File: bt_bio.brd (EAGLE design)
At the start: 57.8 x 57.9 mm, 75 parts, among them U1 ADP121-AUJZ33R7, U2 MCP73837-FCI/UN, U4 ADP121-AUJZ18R7, U5 LSM9DS1, X1 53047-03, X2 MINI-USB-SHIELD-UX60-MB-5ST, X3 53047-03

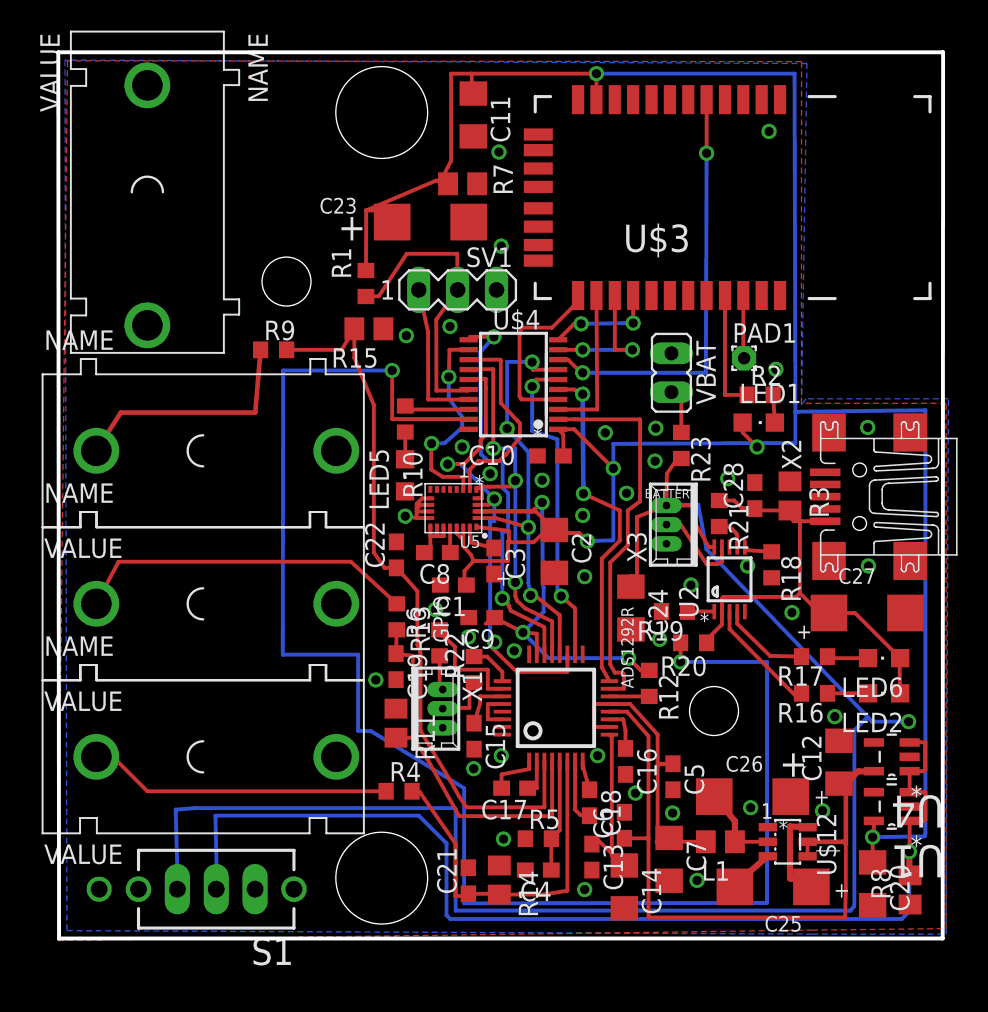
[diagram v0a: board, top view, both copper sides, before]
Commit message: switched to RN4678
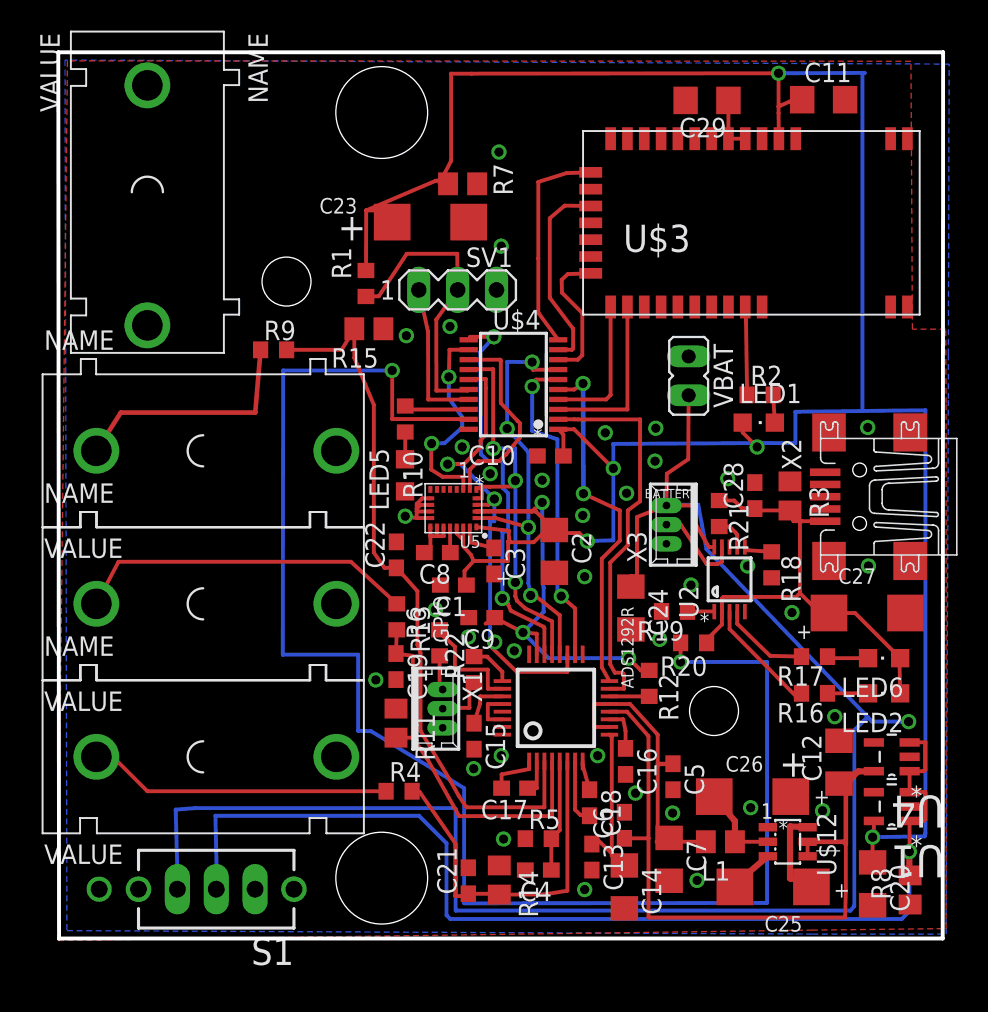
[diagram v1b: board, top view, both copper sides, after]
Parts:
- removed PAD1: WIREPAD1,6/0,8, wirepad:1,6/0,8
- removed R23: 51K, rcl:R0603
- removed U$3: RN42, RN42__BoB:SPARKFUN_RN41
- added C29: 1uF, rcl:C1206
- added U$1: RN4678, rn4678:RN4678
- R2: value 2.2K -> 2K2
- moved C11 22.9 mm to (50.6, 55.5), turned to 0 degrees
- moved VBAT 1.14 mm to (41.8, 37.4)
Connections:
- removed net N$10: R2.1, U$3.21
- removed net N$14: PAD1.1, U$3.22
- removed net N$46: C24.1, R23.2, S1.3, U2.10, X3.1
- removed net N$7: U$3.15, U$4.9
- removed net N$8: U$3.16, U$4.10
- removed net N$9: U$3.5, U$4.8
- new net CTS: U$1.15, U$4.10
- new net RESET: U$1.21, U$4.8
- new net RTS: U$1.17, U$4.9
- new net RX: U$1.22, U$4.4
- new net TX: U$1.23, U$4.3
- net GND: now also C29.2, U$1.1, U$1.2, U$1.20, U$1.3, U$1.31, U$1.32, U$1.33; no longer U$3.1, U$3.12, U$3.28, U$3.29
- net N$2: now also C29.1, U$1.6, U$1.7; no longer U$3.13, U$4.4
- net N$31: now also C24.1, S1.3, U2.10, X3.1; no longer R23.1
- net N$6: now also R2.1, U$1.30; no longer U$3.14, U$4.3
- net V+: now also U$1.4; no longer U$3.11
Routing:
- net N$31: track 3.28 -> 112.4 mm, vias 0 -> 1
- net N$46: track 108.0 -> 0.00 mm, vias 1 -> 0
- net N$9: track 28.0 -> 0.00 mm, vias 2 -> 0
- net CTS: track 0.00 -> 14.3 mm
- net RTS: track 0.00 -> 13.0 mm
- net TX: track 0.00 -> 11.2 mm
- net N$7: track 9.55 -> 0.00 mm, vias 2 -> 0
- net RX: track 0.00 -> 9.30 mm
- net RESET: track 0.00 -> 9.22 mm
- net N$2: track 11.9 -> 3.60 mm
- net N$10: track 7.95 -> 0.00 mm
- net V+: track 192.3 -> 199.8 mm
- net N$8: track 7.13 -> 0.00 mm, vias 2 -> 0
- net N$14: track 4.15 -> 0.00 mm
- net N$6: track 10.0 -> 5.95 mm
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
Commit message: Small fixes in the layout
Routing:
- net GND: vias 36 -> 37
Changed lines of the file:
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@@
 <contactref element="U$1" pad="20"/>
 <contactref element="C29" pad="2"/>
+<via x="33.678" y="45.201" extent="1-16" drill="0.6" shape="octagon"/>
 </signal>
 <signal name="+5V">
@@
 <via x="36.85" y="31.35" extent="1-16" drill="0.6" shape="octagon"/>
 <via x="47.65" y="57.175" extent="1-16" drill="0.6" shape="octagon"/>
-<wire x1="47.65" y1="57.175" x2="53.275" y2="57.2" width="0.254" layer="16"/>
+<wire x1="47.65" y1="57.175" x2="48.2" y2="57.175" width="0.254" layer="16"/>
 <wire x1="48.75" y1="33" x2="46.5000375" y2="33.009621875" width="0.254" layer="16"/>
 <wire x1="46.5000375" y1="33.009621875" x2="36.85" y2="32.95" width="0.254" layer="16"/>
@@
 <wire x1="49.2" y1="55.45" x2="48.375" y2="55.325" width="0.254" layer="1"/>
 <wire x1="48.375" y1="55.325" x2="47.65" y2="55" width="0.254" layer="1"/>
-<wire x1="53.275" y1="57.2" x2="53.131453125" y2="57.2" width="0.254" layer="16"/>
+<wire x1="48.2" y1="57.175" x2="53.131453125" y2="57.2" width="0.254" layer="16"/>
 <wire x1="53.131453125" y1="57.2" x2="53.131453125" y2="35.101546875" width="0.254" layer="16"/>
 </signal>

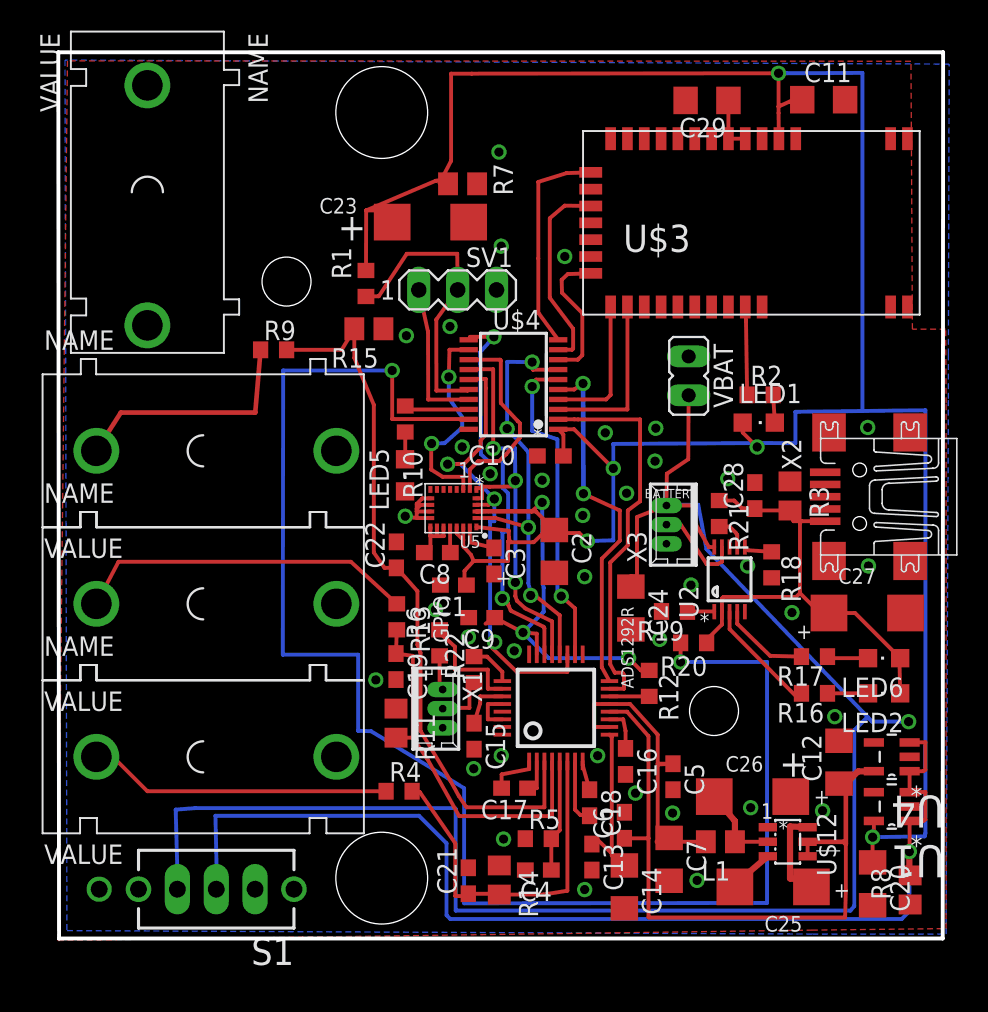
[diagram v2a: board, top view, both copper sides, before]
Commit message: Tested with actual bluetooth module and it seems to work.
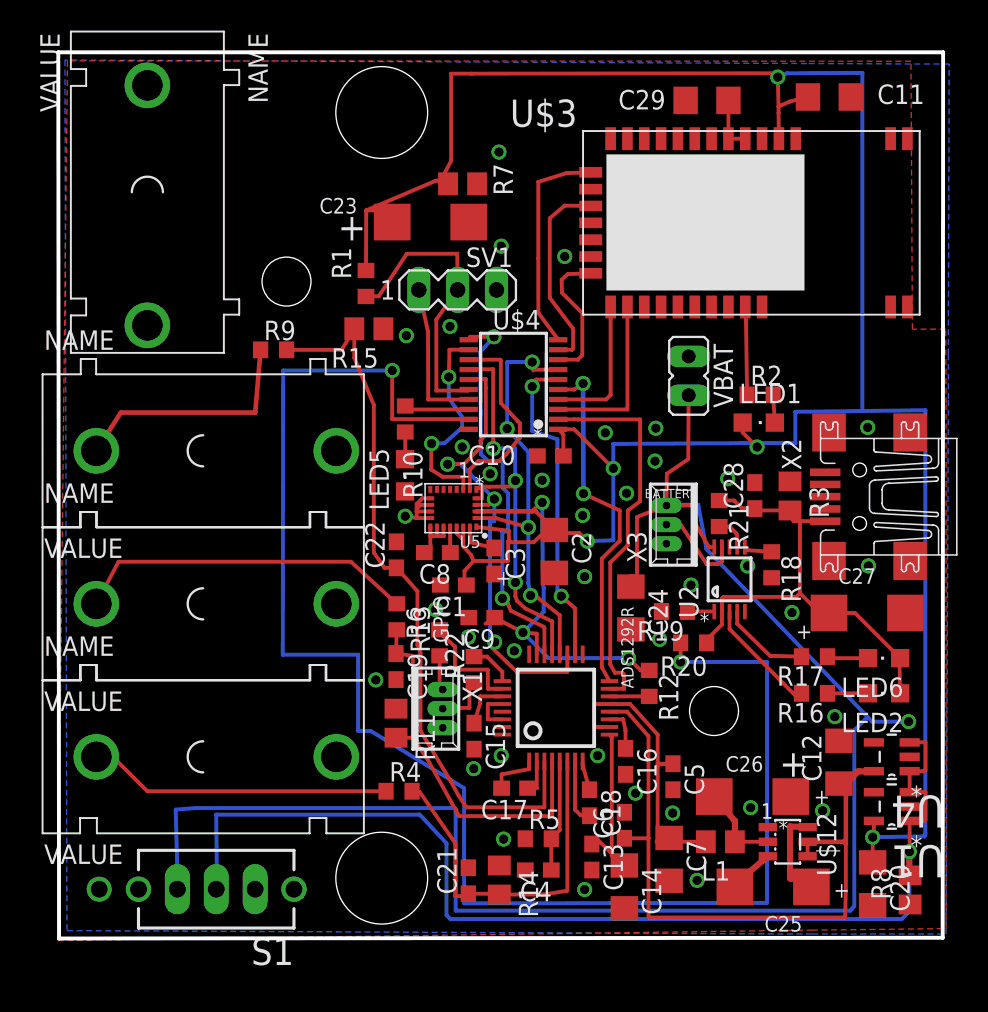
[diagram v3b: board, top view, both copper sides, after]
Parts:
- moved C11 0.41 mm to (51.0, 55.6)
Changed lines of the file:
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@@
 <board>
 <plain>
-<wire x1="0.627" y1="0.627" x2="58.379" y2="0.627" width="0.254" layer="20"/>
-<wire x1="58.379" y1="0.627" x2="58.406" y2="58.545" width="0.254" layer="20"/>
+<wire x1="0.627" y1="0.627" x2="58.379" y2="0.677" width="0.254" layer="20"/>
+<wire x1="58.379" y1="0.677" x2="58.406" y2="58.545" width="0.254" layer="20"/>
 <wire x1="58.406" y1="58.545" x2="0.577" y2="58.545" width="0.254" layer="20"/>
 <wire x1="0.577" y1="58.545" x2="0.627" y2="0.627" width="0.254" layer="20"/>
@@
 <hole x="21.717" y="54.61" drill="6"/>
 <text x="37.55" y="48.2" size="1.778" layer="27">RN42</text>
-<text x="37.5" y="45.5" size="1.778" layer="25">U$3</text>
+<text x="30.1" y="53.675" size="1.778" layer="25">U$3</text>
 <text x="26.7" y="30.75" size="1.016" layer="25">1</text>
 <text x="46.5" y="8.45" size="1.016" layer="25">1</text>
@@
 <text x="38.9" y="29.4" size="0.6096" layer="25">BATTERY</text>
 <text x="26.1" y="19.95" size="1.016" layer="25" rot="R90">GPIO</text>
+<rectangle x1="36.4" y1="42.975" x2="49.35" y2="51.875" layer="25"/>
 </plain>
 <attributes>
@@
 <element name="C12" library="rcl" package="C1206" value="10uF" x="51.6" y="12.15" rot="R90"/>
 <element name="C20" library="rcl" package="C1206" value="10uF" x="53.8" y="4.2" rot="R270"/>
-<element name="C11" library="rcl" package="C1206" value="10uF" x="50.6" y="55.45"/>
+<element name="C11" library="rcl" package="C1206" value="10uF" x="50.975" y="55.625" smashed="yes">
+<attribute name="NAME" x="54.105" y="55.168" size="1.27" layer="25"/>
+<attribute name="VALUE" x="49.705" y="53.212" size="1.27" layer="27"/>
+</element>
 <element name="C23" library="rcl" package="SMC_C" value="4.7uF" x="24.9" y="47.45" smashed="yes">
 <attribute name="NAME" x="17.645" y="48.005" size="1.016" layer="25"/>
@@
 <element name="C24" library="rcl" package="C1206" value="10uF" x="38" y="22.225" rot="R270"/>
 <element name="U$1" library="rn4678" package="RN4678" value="RN4678" x="34.875" y="53.4" rot="R270"/>
-<element name="C29" library="rcl" package="C1206" value="1uF" x="42.975" y="55.4" rot="R180"/>
+<element name="C29" library="rcl" package="C1206" value="1uF" x="42.975" y="55.4" smashed="yes" rot="R180">
+<attribute name="NAME" x="40.27" y="56.082" size="1.27" layer="25" rot="R180"/>
+<attribute name="VALUE" x="44.245" y="57.813" size="1.27" layer="27" rot="R180"/>
+</element>
 </elements>
 <signals>
@@
 <wire x1="33.201" y1="33.876" x2="33.251" y2="33.907" width="0.254" layer="1"/>
 <via x="36.85" y="31.35" extent="1-16" drill="0.6" shape="octagon"/>
-<via x="47.65" y="57.175" extent="1-16" drill="0.6" shape="octagon"/>
-<wire x1="47.65" y1="57.175" x2="48.2" y2="57.175" width="0.254" layer="16"/>
+<via x="47.6" y="56.925" extent="1-16" drill="0.6" shape="octagon"/>
+<wire x1="47.6" y1="56.925" x2="48.2" y2="57.175" width="0.254" layer="16"/>
 <wire x1="48.75" y1="33" x2="46.5000375" y2="33.009621875" width="0.254" layer="16"/>
 <wire x1="46.5000375" y1="33.009621875" x2="36.85" y2="32.95" width="0.254" layer="16"/>
@@
 <wire x1="26.25" y1="57.15" x2="27.6" y2="57.15" width="0.254" layer="1"/>
 <contactref element="U1" pad="5"/>
-<wire x1="27.6" y1="57.15" x2="47.65" y2="57.175" width="0.254" layer="1"/>
+<wire x1="27.6" y1="57.15" x2="47.6" y2="57.175" width="0.254" layer="1"/>
+<wire x1="47.6" y1="57.175" x2="47.6" y2="56.925" width="0.254" layer="1"/>
 <wire x1="20.688" y1="44.286" x2="20.7" y2="48.211" width="0.254" layer="1"/>
 <wire x1="20.7" y1="48.211" x2="25.25" y2="50.15" width="0.254" layer="1"/>
@@
 <wire x1="31.79" y1="28.535" x2="33" y2="27.325" width="0.254" layer="1"/>
 <contactref element="U$1" pad="4"/>
-<wire x1="47.65" y1="57.175" x2="47.65" y2="55" width="0.254" layer="1"/>
+<wire x1="47.6" y1="56.925" x2="47.65" y2="55" width="0.254" layer="1"/>
 <wire x1="47.65" y1="55" x2="47.65" y2="54.575" width="0.254" layer="1"/>
 <wire x1="47.65" y1="54.575" x2="47.675" y2="52.9" width="0.254" layer="1"/>
-<wire x1="49.2" y1="55.45" x2="48.375" y2="55.325" width="0.254" layer="1"/>
+<wire x1="49.575" y1="55.625" x2="48.375" y2="55.325" width="0.254" layer="1"/>
 <wire x1="48.375" y1="55.325" x2="47.65" y2="55" width="0.254" layer="1"/>
 <wire x1="48.2" y1="57.175" x2="53.131453125" y2="57.2" width="0.254" layer="16"/>
@@
 <wire x1="26.2" y1="1.9" x2="25.95" y2="2.15" width="0.254" layer="16"/>
 <wire x1="25.95" y1="2.15" x2="25.95" y2="6.85" width="0.254" layer="16"/>
-<wire x1="25.95" y1="6.85" x2="24.15" y2="8.65" width="0.254" layer="16"/>
-<wire x1="24.15" y1="8.65" x2="10.85" y2="8.65" width="0.254" layer="16"/>
+<wire x1="25.95" y1="6.85" x2="24.2" y2="8.725" width="0.254" layer="16"/>
+<wire x1="24.2" y1="8.725" x2="10.9" y2="8.725" width="0.254" layer="16"/>
 <contactref element="S1" pad="2"/>
-<wire x1="10.85" y1="8.65" x2="10.95" y2="3.9" width="0.254" layer="16"/>
+<wire x1="10.9" y1="8.725" x2="10.95" y2="3.9" width="0.254" layer="16"/>
 <wire x1="10.95" y1="3.9" x2="10.9" y2="3.85" width="0.254" layer="16"/>
 <contactref element="R8" pad="2"/>

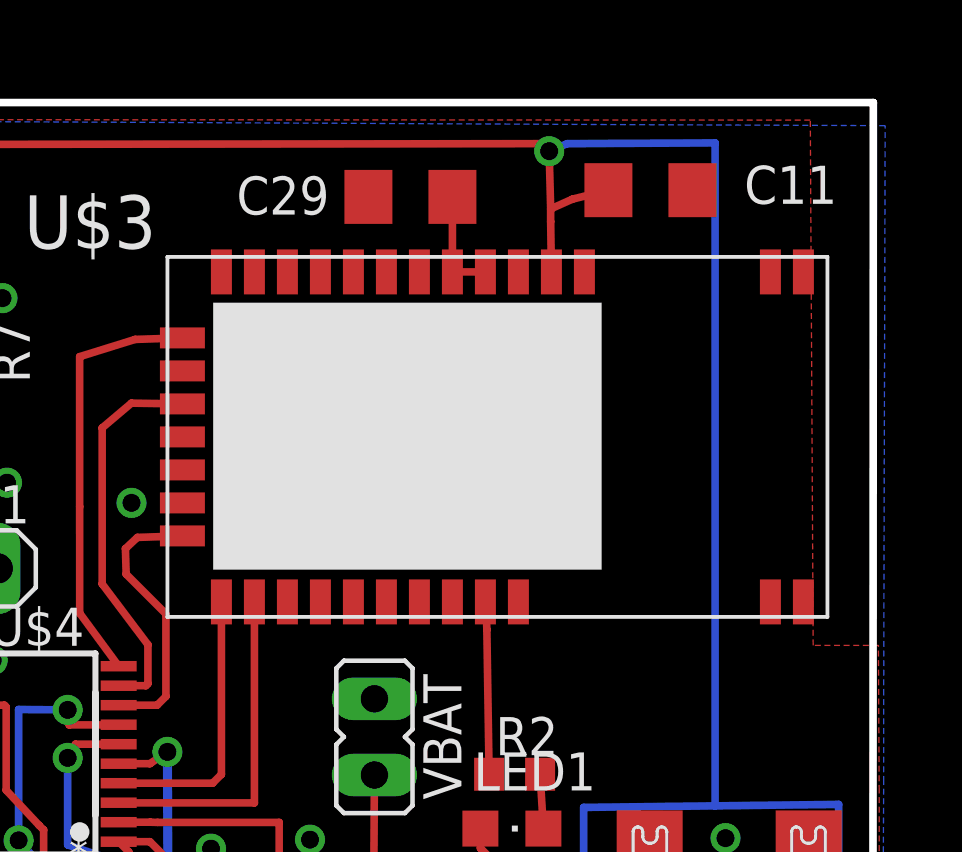
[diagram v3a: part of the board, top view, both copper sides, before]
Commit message: Added more GND vias
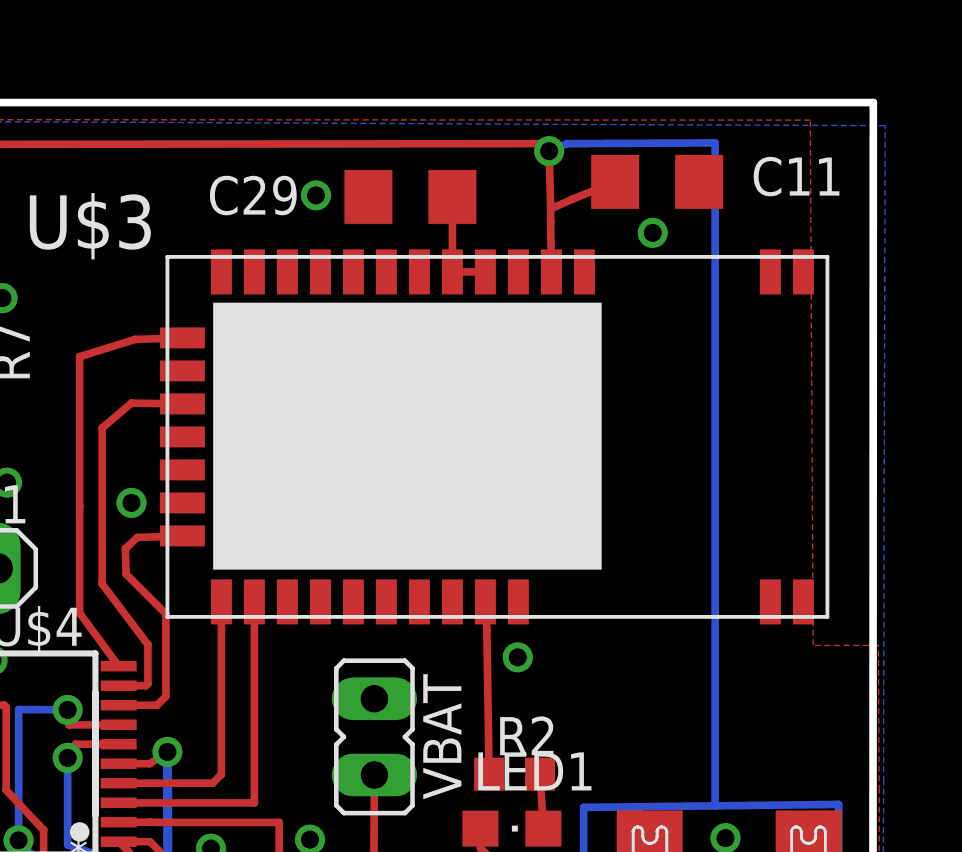
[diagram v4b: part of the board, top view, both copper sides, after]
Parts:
- moved C11 0.36 mm to (51.2, 55.9)
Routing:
- net GND: vias 37 -> 40
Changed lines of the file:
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@@
 <element name="C12" library="rcl" package="C1206" value="10uF" x="51.6" y="12.15" rot="R90"/>
 <element name="C20" library="rcl" package="C1206" value="10uF" x="53.8" y="4.2" rot="R270"/>
-<element name="C11" library="rcl" package="C1206" value="10uF" x="50.975" y="55.625" smashed="yes">
-<attribute name="NAME" x="54.105" y="55.168" size="1.27" layer="25"/>
-<attribute name="VALUE" x="49.705" y="53.212" size="1.27" layer="27"/>
+<element name="C11" library="rcl" package="C1206" value="10uF" x="51.2" y="55.9" smashed="yes">
+<attribute name="NAME" x="54.33" y="55.443" size="1.27" layer="25"/>
+<attribute name="VALUE" x="49.93" y="53.487" size="1.27" layer="27"/>
 </element>
 <element name="C23" library="rcl" package="SMC_C" value="4.7uF" x="24.9" y="47.45" smashed="yes">
@@
 <element name="U$1" library="rn4678" package="RN4678" value="RN4678" x="34.875" y="53.4" rot="R270"/>
 <element name="C29" library="rcl" package="C1206" value="1uF" x="42.975" y="55.4" smashed="yes" rot="R180">
-<attribute name="NAME" x="40.27" y="56.082" size="1.27" layer="25" rot="R180"/>
+<attribute name="NAME" x="39.295" y="56.082" size="1.27" layer="25" rot="R180"/>
 <attribute name="VALUE" x="44.245" y="57.813" size="1.27" layer="27" rot="R180"/>
 </element>
@@
 <contactref element="C29" pad="2"/>
 <via x="33.678" y="45.201" extent="1-16" drill="0.6" shape="octagon"/>
+<via x="39.828" y="55.451" extent="1-16" drill="0.6" shape="octagon"/>
+<via x="46.553" y="40.051" extent="1-16" drill="0.6" shape="octagon"/>
+<via x="51.053" y="54.201" extent="1-16" drill="0.6" shape="octagon"/>
 </signal>
 <signal name="+5V">
@@
 <wire x1="47.65" y1="55" x2="47.65" y2="54.575" width="0.254" layer="1"/>
 <wire x1="47.65" y1="54.575" x2="47.675" y2="52.9" width="0.254" layer="1"/>
-<wire x1="49.575" y1="55.625" x2="48.375" y2="55.325" width="0.254" layer="1"/>
+<wire x1="49.8" y1="55.9" x2="48.375" y2="55.325" width="0.254" layer="1"/>
 <wire x1="48.375" y1="55.325" x2="47.65" y2="55" width="0.254" layer="1"/>
 <wire x1="48.2" y1="57.175" x2="53.131453125" y2="57.2" width="0.254" layer="16"/>
